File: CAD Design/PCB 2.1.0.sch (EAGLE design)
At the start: 49 parts, among them U1 CC2538, U2 MAX1555, X1 32MHz, X2 FC-12M

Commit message: Board update
Added Vbatt pads, ground plane, ready to route
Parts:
- added H1, H2: MOUNT-PAD-SQUARE2.8, holes:MOUNT-PAD-SQUARE2.8
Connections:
- net GND: now also H2.MOUNT
- net N$14: now also H1.MOUNT
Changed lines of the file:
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@@
 <part name="C5" library="discrete" deviceset="C" device="C0402" value="1n"/>
 <part name="C14" library="discrete" deviceset="C" device="C0402" value="0u1"/>
+<part name="GND10" library="supply1" deviceset="GND" device=""/>
+<part name="H1" library="holes" deviceset="MOUNT-PAD-SQUARE" device="2.8"/>
+<part name="H2" library="holes" deviceset="MOUNT-PAD-SQUARE" device="2.8"/>
 </parts>
 <sheets>
@@
 <instance part="C5" gate="C" x="152.4" y="53.34" rot="R270"/>
 <instance part="C14" gate="C" x="86.36" y="53.34" rot="R90"/>
+<instance part="GND10" gate="1" x="83.82" y="134.62" rot="R180"/>
+<instance part="H1" gate="G$1" x="68.58" y="129.54" rot="R270"/>
+<instance part="H2" gate="G$1" x="83.82" y="129.54" rot="R270"/>
 </instances>
 <busses>
@@
 <pinref part="C5" gate="C" pin="1"/>
 </segment>
+<segment>
+<pinref part="GND10" gate="1" pin="GND"/>
+<pinref part="H2" gate="G$1" pin="MOUNT"/>
+</segment>
 </net>
 <net name="3V3" class="0">
@@
 <pinref part="C13" gate="C" pin="2"/>
 <pinref part="C1" gate="C" pin="1"/>
-</segment>
-</net>
+<pinref part="H1" gate="G$1" pin="MOUNT"/>
+</segment>
+</net>

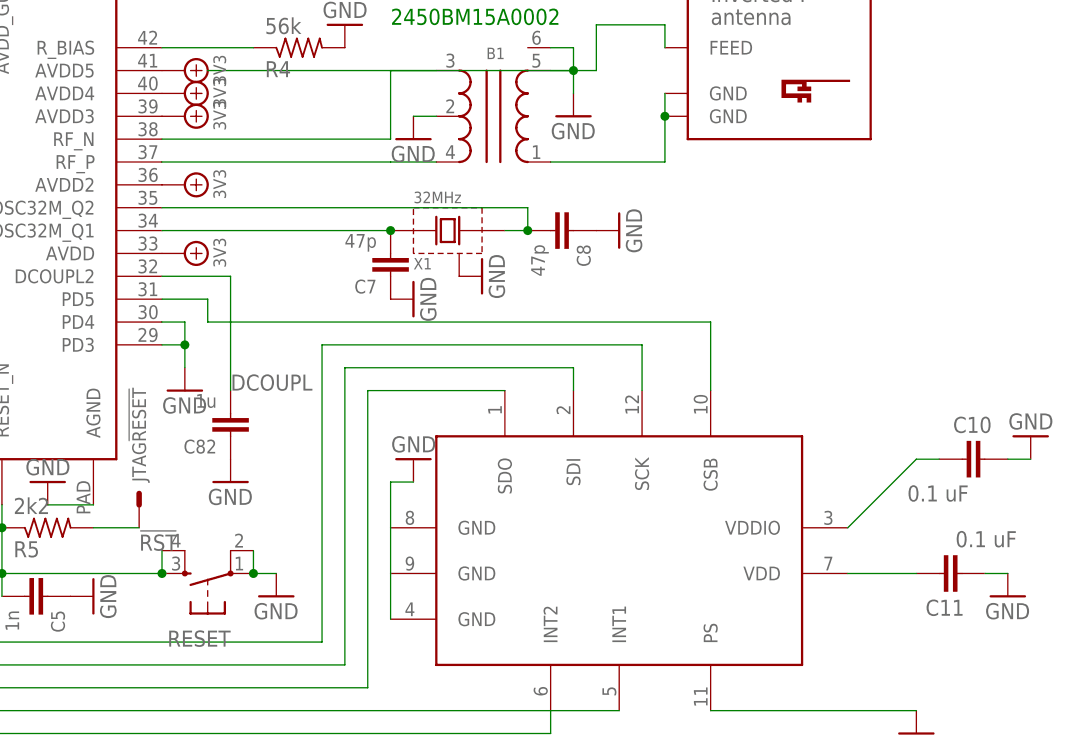
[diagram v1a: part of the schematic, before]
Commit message: 3/16/14 AM fixes
Tweaked schematic as per Jeff’s audit.  Begun re-orienting parts on
board.
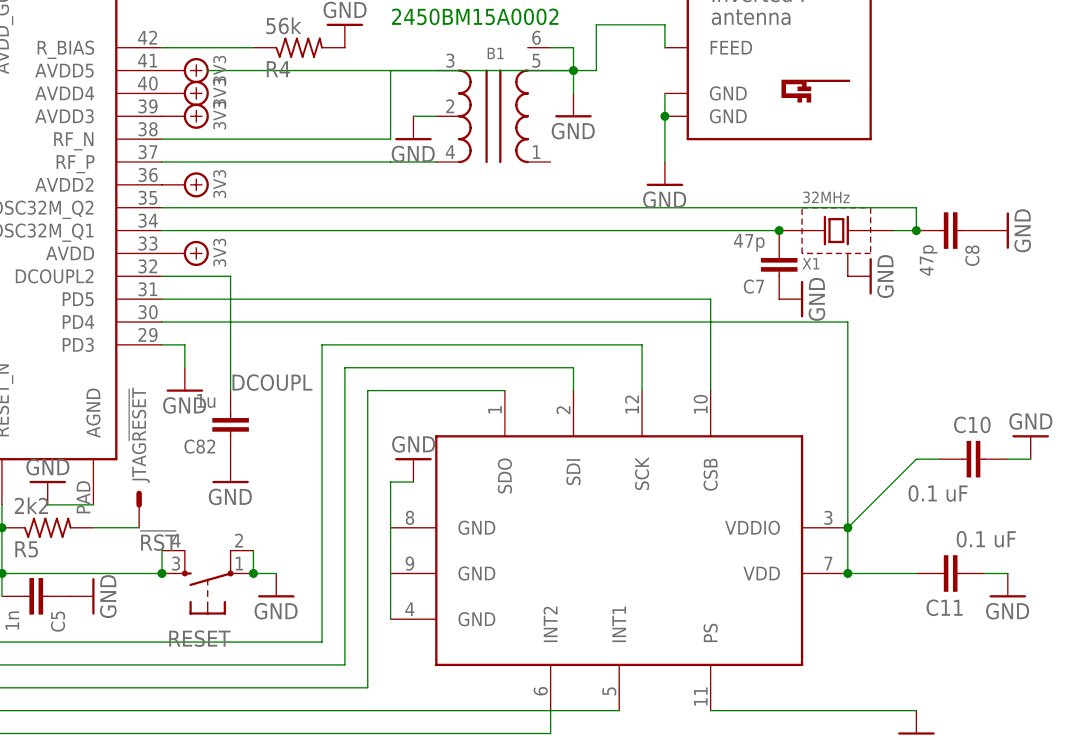
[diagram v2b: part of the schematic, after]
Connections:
- removed net RF: B1.1, U$2.GND, U$2.GND@1
- removed net VDD: C11.1, U$1.VDD
- removed net VDDIO: C10.2, U$1.VDDIO
- new net N$45: C10.2, C11.1, U$1.VDD, U$1.VDDIO, U1.PD4
- net GND: now also U$2.GND, U$2.GND@1; no longer U1.PD4
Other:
- moved on the sheet: C7, C8, X1
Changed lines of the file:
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@@
 <part name="H1" library="holes" deviceset="MOUNT-PAD-SQUARE" device="2.8"/>
 <part name="H2" library="holes" deviceset="MOUNT-PAD-SQUARE" device="2.8"/>
+<part name="GND34" library="supply1" deviceset="GND" device=""/>
 </parts>
 <sheets>
@@
 <instance part="GND12" gate="1" x="193.04" y="104.14"/>
 <instance part="GND13" gate="1" x="210.82" y="106.68"/>
-<instance part="X1" gate="G$1" x="195.58" y="93.98"/>
-<instance part="GND14" gate="1" x="200.66" y="88.9" rot="R90"/>
-<instance part="C7" gate="C" x="190.5" y="88.9" rot="R180"/>
-<instance part="C8" gate="C" x="210.82" y="93.98" rot="R270"/>
-<instance part="GND15" gate="1" x="215.9" y="93.98" rot="R90"/>
-<instance part="GND16" gate="1" x="193.04" y="86.36" rot="R90"/>
+<instance part="X1" gate="G$1" x="238.76" y="93.98"/>
+<instance part="GND14" gate="1" x="243.84" y="88.9" rot="R90"/>
+<instance part="C7" gate="C" x="233.68" y="88.9" rot="R180"/>
+<instance part="C8" gate="C" x="254" y="93.98" rot="R270"/>
+<instance part="GND15" gate="1" x="259.08" y="93.98" rot="R90"/>
+<instance part="GND16" gate="1" x="236.22" y="86.36" rot="R90"/>
 <instance part="JTAG" gate="-VDD_IO" x="170.18" y="139.7" smashed="yes">
 <attribute name="NAME" x="172.72" y="138.938" size="1.524" layer="95"/>
@@
 <instance part="H1" gate="G$1" x="68.58" y="129.54" rot="R270"/>
 <instance part="H2" gate="G$1" x="83.82" y="129.54" rot="R270"/>
+<instance part="GND34" gate="1" x="220.98" y="99.06"/>
 </instances>
 <busses>
@@
 </segment>
 <segment>
-<pinref part="U1" gate="G$1" pin="PD4"/>
-<wire x1="165.1" y1="83.82" x2="167.64" y2="83.82" width="0.1524" layer="91"/>
-<wire x1="167.64" y1="83.82" x2="167.64" y2="81.28" width="0.1524" layer="91"/>
 <pinref part="U1" gate="G$1" pin="PD3"/>
 <wire x1="167.64" y1="81.28" x2="167.64" y2="78.74" width="0.1524" layer="91"/>
 <wire x1="165.1" y1="81.28" x2="167.64" y2="81.28" width="0.1524" layer="91"/>
-<junction x="167.64" y="81.28"/>
 <pinref part="GND33" gate="1" pin="GND"/>
 </segment>
@@
 <pinref part="GND10" gate="1" pin="GND"/>
 <pinref part="H2" gate="G$1" pin="MOUNT"/>
+</segment>
+<segment>
+<pinref part="U$2" gate="G$1" pin="GND"/>
+<wire x1="220.98" y1="101.6" x2="220.98" y2="106.68" width="0.1524" layer="91"/>
+<pinref part="U$2" gate="G$1" pin="GND@1"/>
+<junction x="220.98" y="106.68"/>
+<wire x1="220.98" y1="106.68" x2="220.98" y2="109.22" width="0.1524" layer="91"/>
+<pinref part="GND34" gate="1" pin="GND"/>
 </segment>
 </net>
@@
 </segment>
 </net>
-<net name="RF" class="0">
-<segment>
-<pinref part="B1" gate="G$1" pin="1"/>
-<wire x1="220.98" y1="101.6" x2="208.28" y2="101.6" width="0.1524" layer="91"/>
-<pinref part="U$2" gate="G$1" pin="GND"/>
-<wire x1="220.98" y1="101.6" x2="220.98" y2="106.68" width="0.1524" layer="91"/>
-<pinref part="U$2" gate="G$1" pin="GND@1"/>
-<junction x="220.98" y="106.68"/>
-<wire x1="220.98" y1="106.68" x2="220.98" y2="109.22" width="0.1524" layer="91"/>
-</segment>
-</net>
 <net name="N$30" class="0">
 <segment>
 <pinref part="U1" gate="G$1" pin="XOSC32M_Q2"/>
-<wire x1="165.1" y1="96.52" x2="205.74" y2="96.52" width="0.1524" layer="91"/>
-<wire x1="205.74" y1="96.52" x2="205.74" y2="93.98" width="0.1524" layer="91"/>
+<wire x1="165.1" y1="96.52" x2="248.92" y2="96.52" width="0.1524" layer="91"/>
+<wire x1="248.92" y1="96.52" x2="248.92" y2="93.98" width="0.1524" layer="91"/>
 <pinref part="X1" gate="G$1" pin="X2"/>
 <pinref part="C8" gate="C" pin="2"/>
-<junction x="205.74" y="93.98"/>
-<wire x1="205.74" y1="93.98" x2="203.2" y2="93.98" width="0.1524" layer="91"/>
+<junction x="248.92" y="93.98"/>
+<wire x1="248.92" y1="93.98" x2="246.38" y2="93.98" width="0.1524" layer="91"/>
 </segment>
 </net>
@@
 <pinref part="X1" gate="G$1" pin="X1"/>
 <pinref part="U1" gate="G$1" pin="XOSC32M_Q1"/>
-<wire x1="190.5" y1="93.98" x2="165.1" y2="93.98" width="0.1524" layer="91"/>
+<wire x1="233.68" y1="93.98" x2="165.1" y2="93.98" width="0.1524" layer="91"/>
 <pinref part="C7" gate="C" pin="2"/>
-<junction x="190.5" y="93.98"/>
+<junction x="233.68" y="93.98"/>
 </segment>
 </net>
@@
 </segment>
 </net>
-<net name="VDDIO" class="0">
-<segment>
-<wire x1="251.46" y1="68.58" x2="248.92" y2="68.58" width="0.1524" layer="91"/>
-<wire x1="248.92" y1="68.58" x2="241.3" y2="60.96" width="0.1524" layer="91"/>
-<pinref part="C10" gate="G$1" pin="2"/>
-<pinref part="U$1" gate="G$1" pin="VDDIO"/>
-</segment>
-</net>
-<net name="VDD" class="0">
-<segment>
-<wire x1="248.92" y1="55.88" x2="241.3" y2="55.88" width="0.1524" layer="91"/>
-<pinref part="C11" gate="G$1" pin="1"/>
-<pinref part="U$1" gate="G$1" pin="VDD"/>
-</segment>
-</net>
 <net name="N$9" class="0">
 <segment>
@@
 <segment>
 <pinref part="U$1" gate="G$1" pin="CSB"/>
-<wire x1="226.06" y1="76.2" x2="226.06" y2="83.82" width="0.1524" layer="91"/>
-<wire x1="226.06" y1="83.82" x2="170.18" y2="83.82" width="0.1524" layer="91"/>
-<wire x1="170.18" y1="83.82" x2="170.18" y2="86.36" width="0.1524" layer="91"/>
+<wire x1="226.06" y1="76.2" x2="226.06" y2="86.36" width="0.1524" layer="91"/>
+<wire x1="226.06" y1="86.36" x2="165.1" y2="86.36" width="0.1524" layer="91"/>
 <pinref part="U1" gate="G$1" pin="PD5"/>
-<wire x1="170.18" y1="86.36" x2="165.1" y2="86.36" width="0.1524" layer="91"/>
 </segment>
 </net>
@@
 </segment>
 </net>
+<net name="N$45" class="0">
+<segment>
+<wire x1="248.92" y1="55.88" x2="241.3" y2="55.88" width="0.1524" layer="91"/>
+<pinref part="C11" gate="G$1" pin="1"/>
+<pinref part="U$1" gate="G$1" pin="VDD"/>
+<wire x1="251.46" y1="68.58" x2="248.92" y2="68.58" width="0.1524" layer="91"/>
+<wire x1="248.92" y1="68.58" x2="241.3" y2="60.96" width="0.1524" layer="91"/>
+<pinref part="C10" gate="G$1" pin="2"/>
+<pinref part="U$1" gate="G$1" pin="VDDIO"/>
+<wire x1="241.3" y1="55.88" x2="241.3" y2="60.96" width="0.1524" layer="91"/>
+<wire x1="241.3" y1="60.96" x2="241.3" y2="83.82" width="0.1524" layer="91"/>
+<pinref part="U1" gate="G$1" pin="PD4"/>
+<wire x1="241.3" y1="83.82" x2="165.1" y2="83.82" width="0.1524" layer="91"/>
+<junction x="241.3" y="60.96"/>
+<junction x="241.3" y="55.88"/>
+</segment>
+</net>

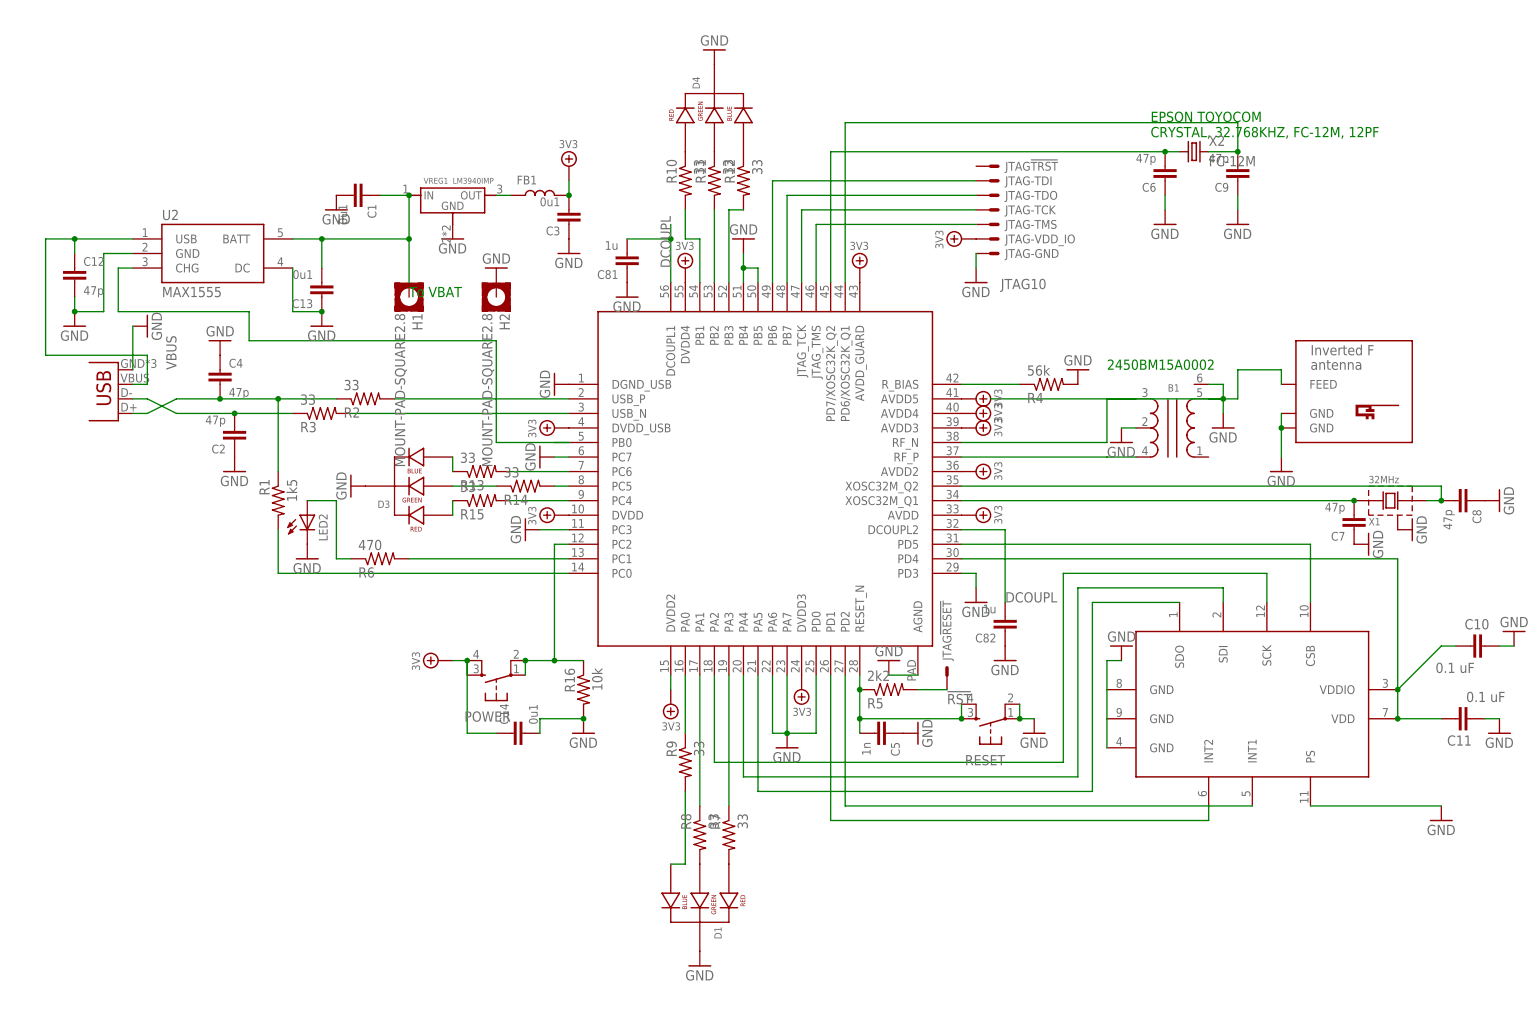
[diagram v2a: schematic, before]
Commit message: Midday Push
Manual routing ~50% complete.  Needs new accelerometer, yet to
integrate LED driver.
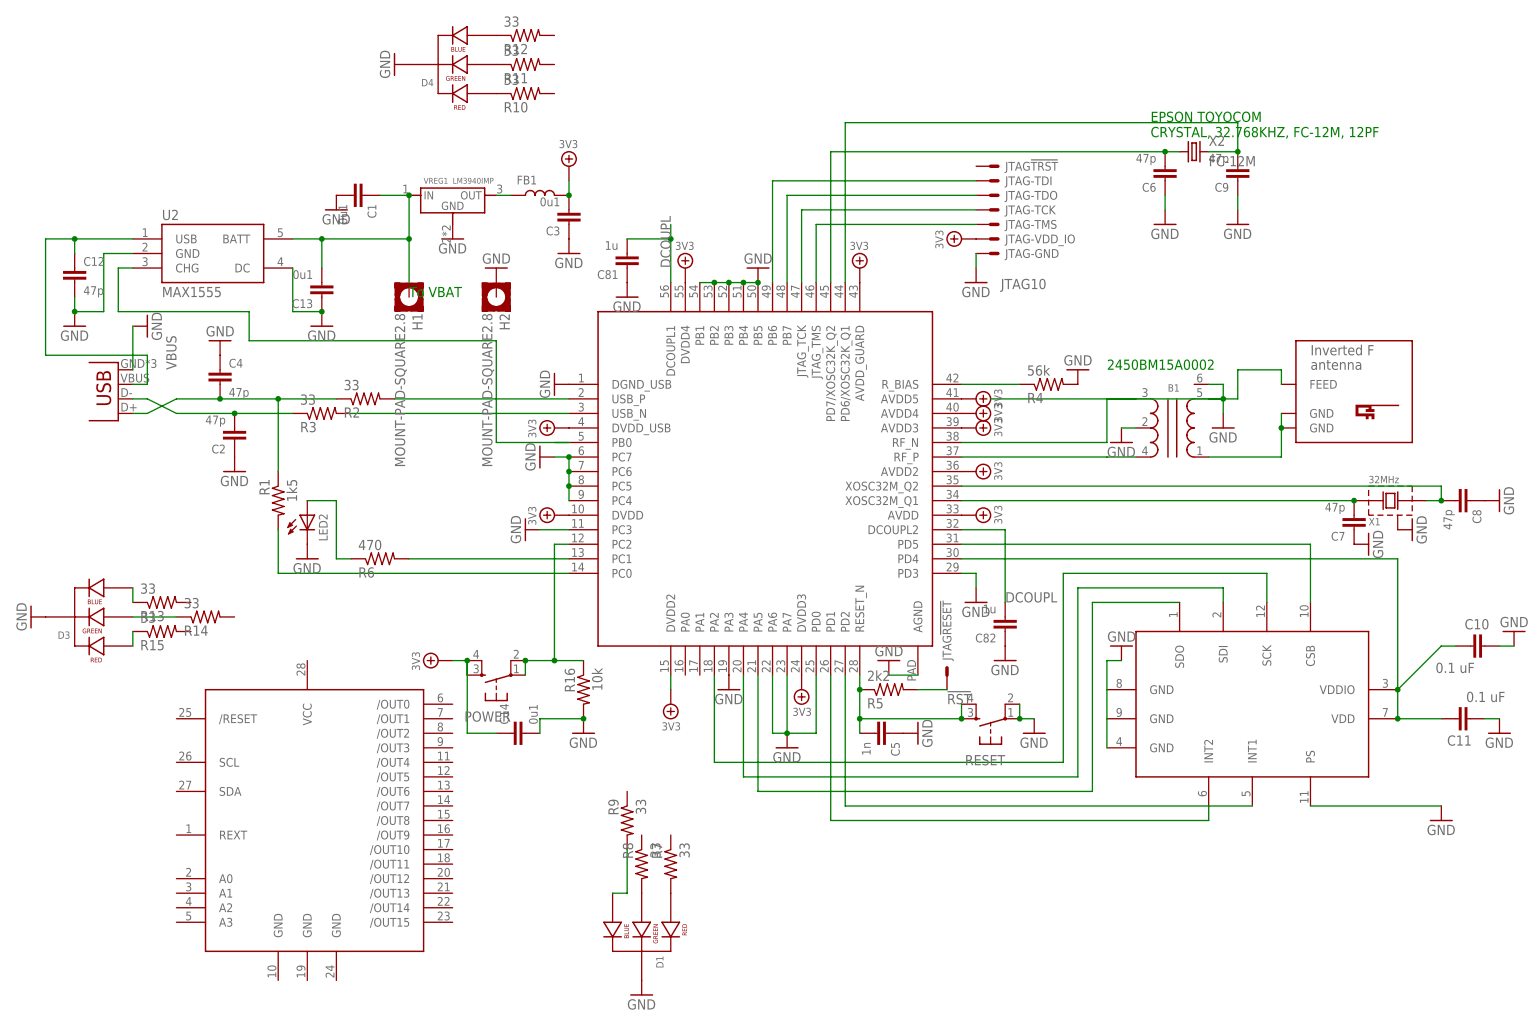
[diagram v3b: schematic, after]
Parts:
- added U$3: TLC59116, tlc59116:TLC59116
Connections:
- removed net N$19: R10.2, U1.PB1
- removed net N$20: R11.2, U1.PB2
- removed net N$22: R12.2, U1.PB3
- removed net N$33: R15.2, U1.PC4
- removed net N$34: R14.2, U1.PC5
- removed net N$36: R13.2, U1.PC6
- removed net N$37: R9.1, U1.PA0
- removed net N$38: R8.1, U1.PA1
- removed net N$39: R7.1, U1.PA3
- new net RF: B1.1, U$2.GND, U$2.GND@1
- net GND: now also U1.PA3, U1.PB1, U1.PB2, U1.PB3, U1.PC4, U1.PC5, U1.PC6; no longer U$2.GND, U$2.GND@1
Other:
- moved on the sheet: D1, D3, D4, R10, R11, R12, R13, R14, R15, R7, R8, R9
